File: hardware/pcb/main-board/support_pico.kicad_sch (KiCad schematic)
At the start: 8 parts, among them J701 DE15_Receptacle_HighDensity_M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, J702 Z88 SD Card, U701 Support Pico

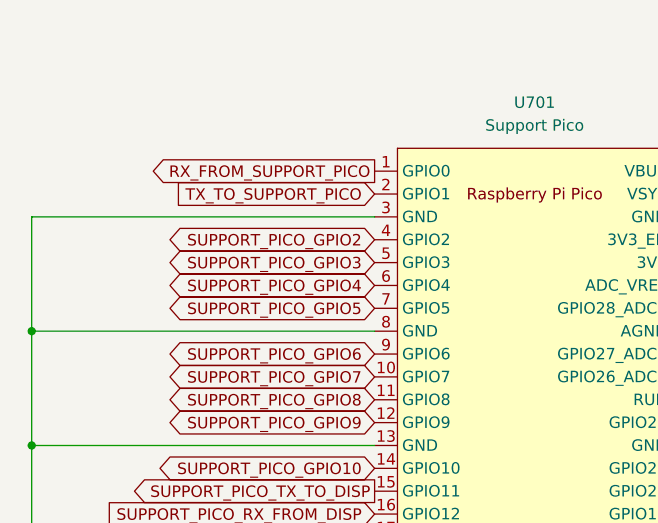
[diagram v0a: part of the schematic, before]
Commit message: start next board iteration, add latch and pico power bits
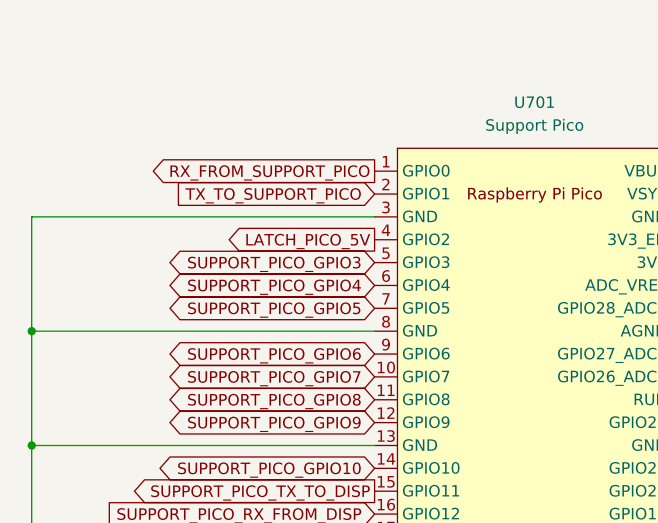
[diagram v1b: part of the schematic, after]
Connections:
- net SUPPORT_PICO_GPIO2: no longer U701.4 (GPIO2)
- new net LATCH_PICO_5V: U701.4 (GPIO2)
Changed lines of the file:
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@@
 	(title_block
 		(title "Z88R - Z88 Recreated")
-		(date "2024-08-23")
-		(rev "20240823")
+		(date "2025-12-19")
+		(rev "20251219WIP")
 		(company "Fountain and Menadue")
 	)
@@
 		)
 	)
-	(global_label "SUPPORT_PICO_GPIO2"
-		(shape bidirectional)
+	(global_label "LATCH_PICO_5V"
+		(shape output)
 		(at 58.42 43.18 180)
 		(fields_autoplaced yes)
@@
 		)
 		(property "Intersheetrefs" "${INTERSHEET_REFS}"
-			(at 34.3931 43.18 0)
+			(at 41.6956 43.18 0)
 			(effects
 				(font
@@
 		(shape output)
 		(at 58.42 76.2 180)
-		(fields_autoplaced yes)
 		(effects
 			(font
@@
 		(shape input)
 		(at 226.06 118.11 180)
-		(fields_autoplaced yes)
 		(effects
 			(font
@@
 		(shape output)
 		(at 58.42 83.82 180)
-		(fields_autoplaced yes)
 		(effects
 			(font
@@
 		(shape input)
 		(at 93.98 63.5 0)
-		(fields_autoplaced yes)
 		(effects
 			(font
@@
 		(shape input)
 		(at 93.98 68.58 0)
-		(fields_autoplaced yes)
 		(effects
 			(font
@@
 		(shape input)
 		(at 226.06 124.46 180)
-		(fields_autoplaced yes)
 		(effects
 			(font
@@
 		(shape output)
 		(at 58.42 81.28 180)
-		(fields_autoplaced yes)
-		(effects
-			(font
+		(effects
+			(font

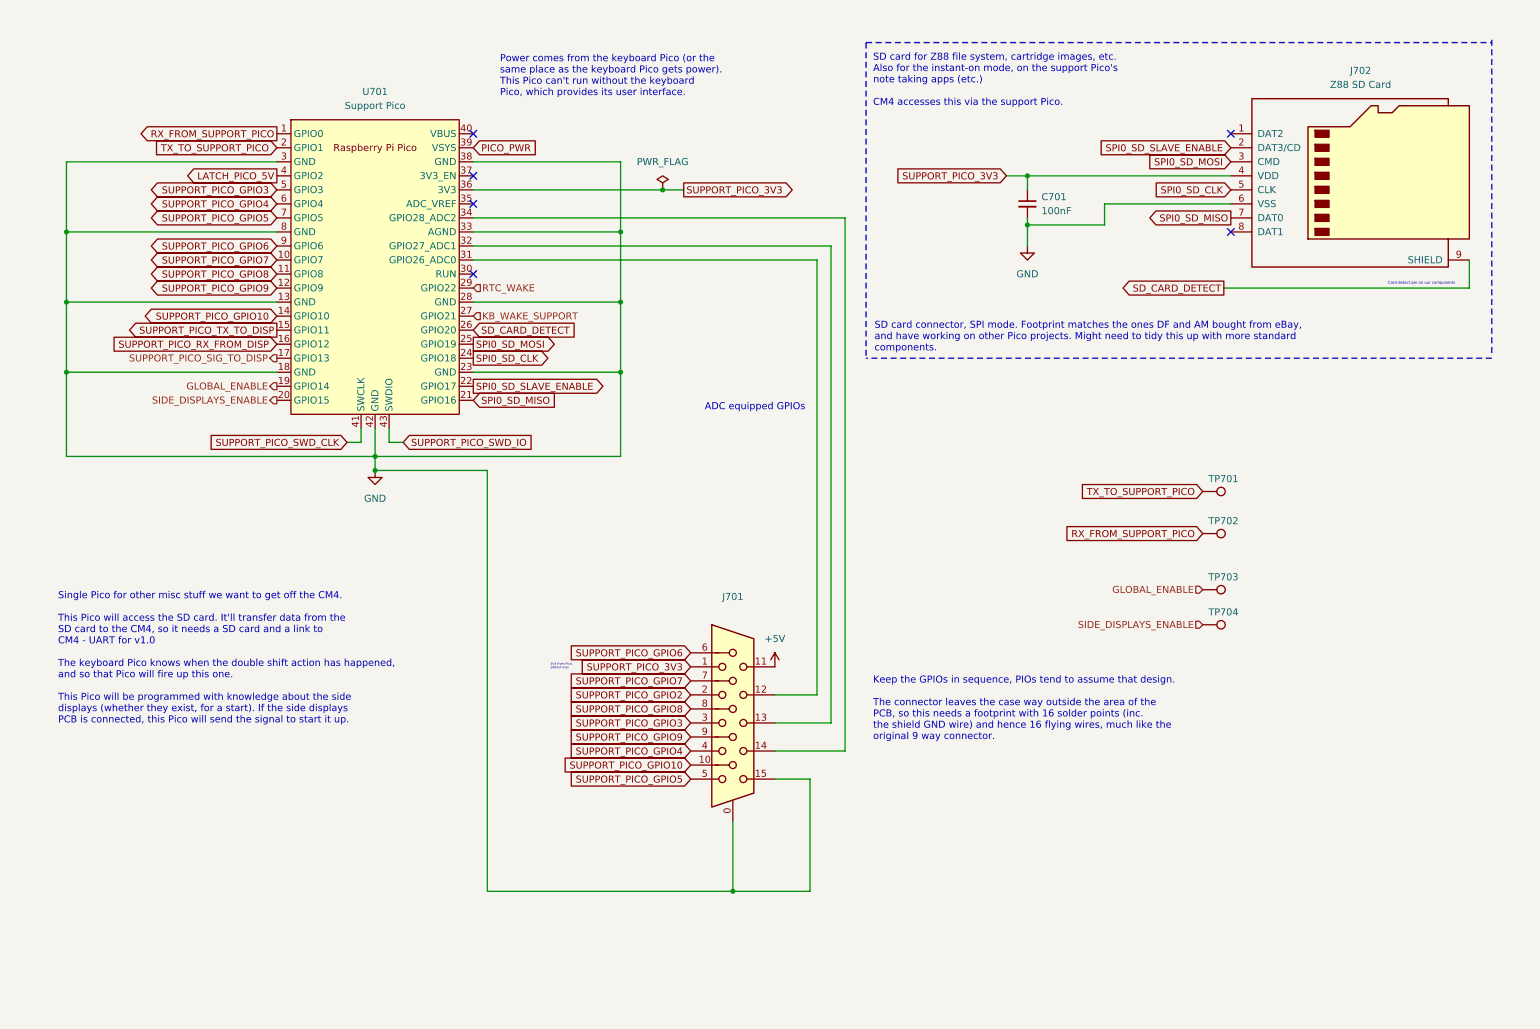
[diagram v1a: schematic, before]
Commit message: CM4 power switch
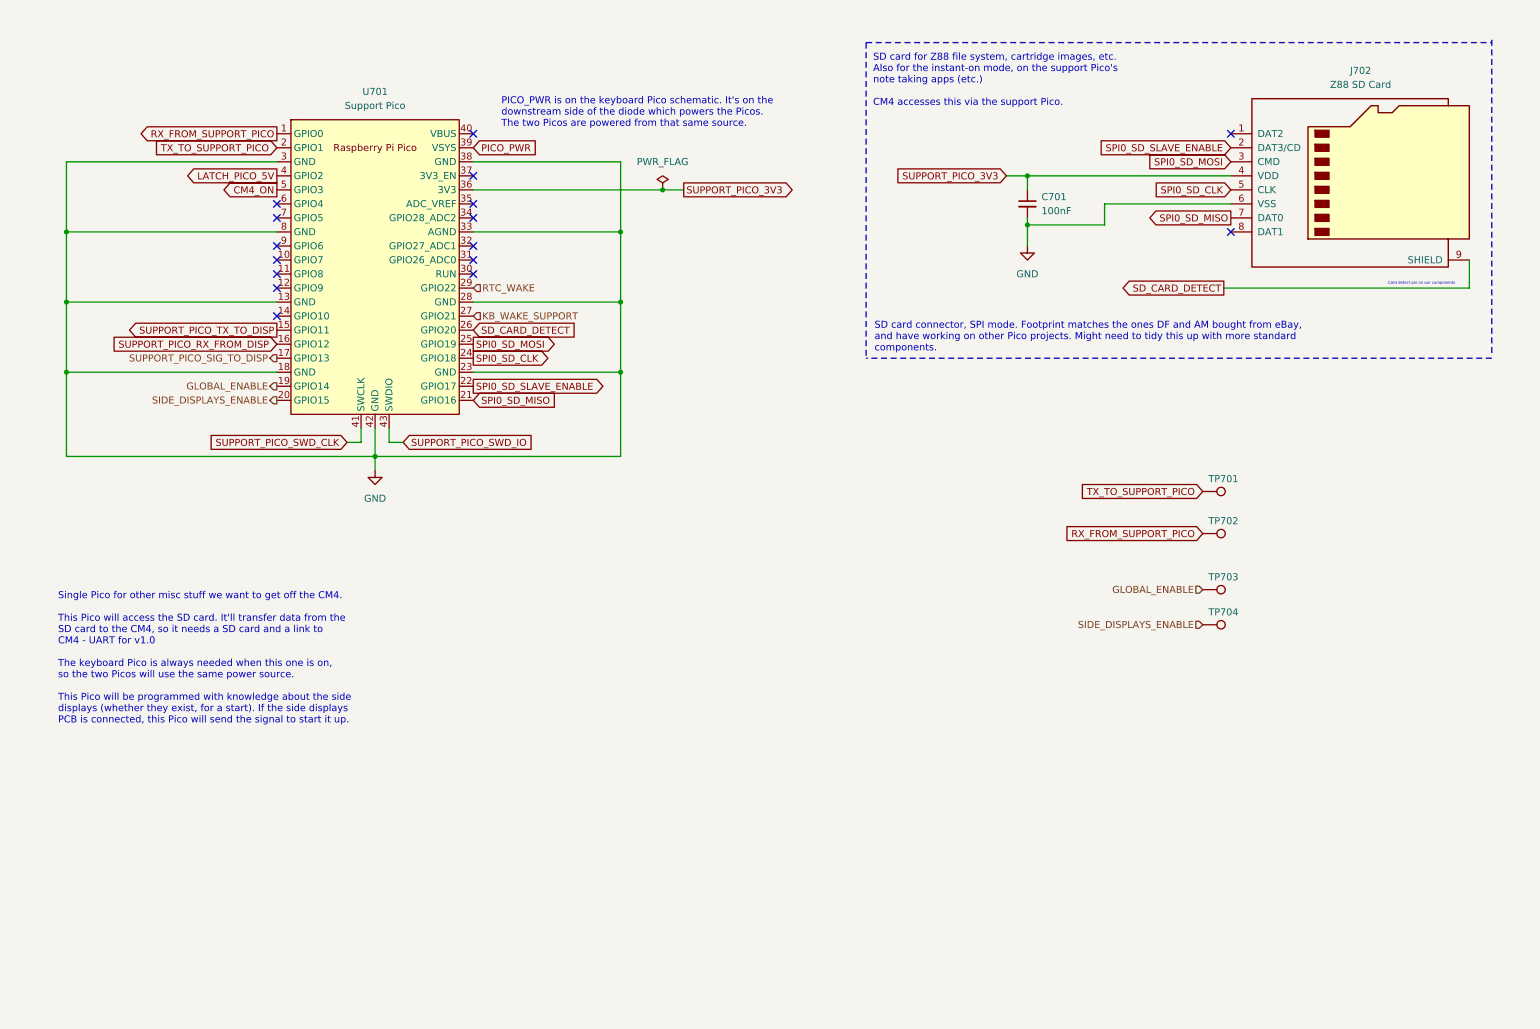
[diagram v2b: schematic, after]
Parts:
- removed J701: DE15_Receptacle_HighDensity_MountingHoles, Connector_Dsub:DSUB-15-HD_Female_Vertical_P2.29x1.98mm_MountingHoles, symbol Connector:DE15_Receptacle_HighDensity_MountingHoles
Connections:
- net SUPPORT_PICO_GPIO10: no longer names the net of U701.14 (GPIO10)
- net SUPPORT_PICO_GPIO3 renamed CM4_ON
- net SUPPORT_PICO_GPIO4: no longer names the net of U701.6 (GPIO4)
- net SUPPORT_PICO_GPIO5: no longer names the net of U701.7 (GPIO5)
- net SUPPORT_PICO_GPIO6: no longer names the net of U701.9 (GPIO6)
- net SUPPORT_PICO_GPIO7: no longer names the net of U701.10 (GPIO7)
- net SUPPORT_PICO_GPIO8: no longer names the net of U701.11 (GPIO8)
- net SUPPORT_PICO_GPIO9: no longer names the net of U701.12 (GPIO9)
- no-connect marks 6 -> 16
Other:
- note added: "PICO_PWR is on the keyboard Pico schematic. It's on the downstream side of the diode which powers the Picos. The two Picos are powered from that same source."
- note added: "Single Pico for other misc stuff we want to get off the CM4. This Pico will access the SD card. It'll transfer data from the SD card to the CM4, so it needs a SD card and a link to CM4 - UART for v1.0 The keyboard Pico is always needed when this one is on, so the two Picos will use the same power source. This Pico will be programmed with knowledge about the side displays (whether they exist, for 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"
- note removed: "3V3 from Pico, 300mA max"
- note removed: "ADC equipped GPIOs"
- note removed: "Keep the GPIOs in sequence, PIOs tend to assume that design. The connector leaves the case way outside the area of the PCB, so this needs a footprint with 16 solder points (inc. the shield GND wire) and hence 16 flying wires, much like the original 9 way connector."
- note removed: "Power comes from the keyboard Pico (or the same place as the keyboard Pico gets power). This Pico can't run without the keyboard Pico, which provides its user interface."
- note removed: "Single Pico for other misc stuff we want to get off the CM4. This Pico will access the SD card. It'll transfer data from the SD card to the CM4, so it needs a SD card and a link to CM4 - UART for v1.0 The keyboard Pico knows when the double shift action has happened, and so that Pico will fire up this one. This Pico will be programmed with knowledge about the side displays (whether they exist, fo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"

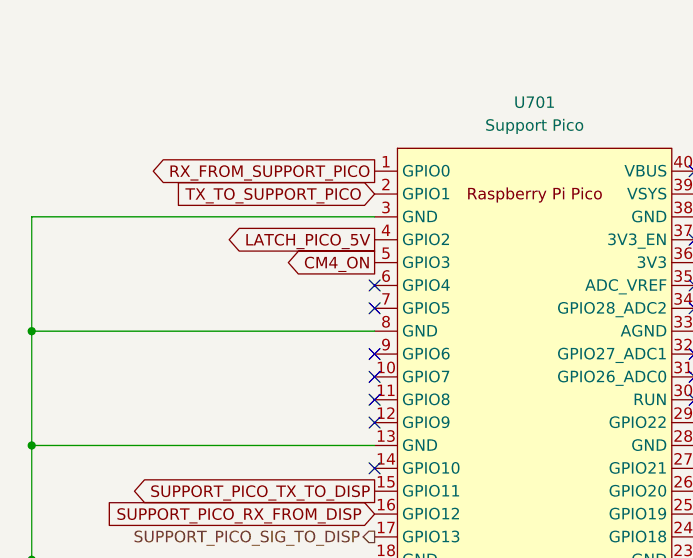
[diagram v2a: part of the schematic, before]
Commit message: add i2c connection to the support pico so it can control the RTC
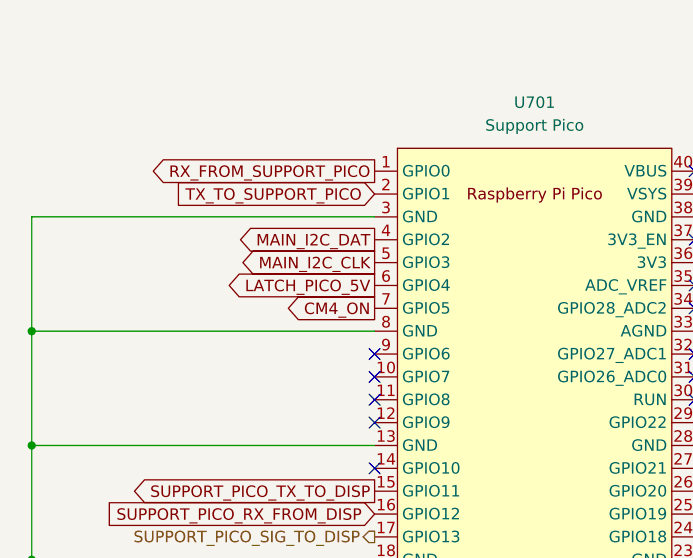
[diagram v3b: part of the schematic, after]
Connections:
- net CM4_ON: now also U701.7 (GPIO5); no longer U701.5 (GPIO3)
- net LATCH_PICO_5V: now also U701.6 (GPIO4); no longer U701.4 (GPIO2)
- new net MAIN_I2C_CLK: U701.5 (GPIO3)
- new net MAIN_I2C_DAT: U701.4 (GPIO2)
- no-connect marks 16 -> 14
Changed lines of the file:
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@@
-	)
-	(no_connect
-		(at 58.42 48.26)
 	)
 	(no_connect
@@
 	(no_connect
 		(at 58.42 55.88)
-	)
-	(no_connect
-		(at 58.42 50.8)
 	)
 	(no_connect
@@
 	(global_label "LATCH_PICO_5V"
 		(shape output)
-		(at 58.42 43.18 180)
-		(fields_autoplaced yes)
-		(effects
-			(font
-				(size 1.27 1.27)
-			)
-			(justify right)
-		)
-		(property "Intersheetrefs" "${INTERSHEET_REFS}"
-			(at 41.6956 43.18 0)
+		(at 58.42 48.26 180)
+		(fields_autoplaced yes)
+		(effects
+			(font
+				(size 1.27 1.27)
+			)
+			(justify right)
+		)
+		(property "Intersheetrefs" "${INTERSHEET_REFS}"
+			(at 41.6956 48.26 0)
 			(effects
 				(font
@@
 		)
 	)
+	(global_label "MAIN_I2C_DAT"
+		(shape output)
+		(at 58.42 43.18 180)
+		(fields_autoplaced yes)
+		(effects
+			(font
+				(size 1.27 1.27)
+			)
+			(justify right)
+		)
+		(property "Intersheetrefs" "${INTERSHEET_REFS}"
+			(at 43.268 43.18 0)
+			(effects
+				(font
+					(size 1.27 1.27)
+				)
+				(justify right)
+				(hide yes)
+			)
+		)
+	)
 	(global_label "SUPPORT_PICO_SWD_IO"
 		(shape input)
@@
 		)
 	)
+	(global_label "MAIN_I2C_CLK"
+		(shape output)
+		(at 58.42 45.72 180)
+		(fields_autoplaced yes)
+		(effects
+			(font
+				(size 1.27 1.27)
+			)
+			(justify right)
+		)
+		(property "Intersheetrefs" "${INTERSHEET_REFS}"
+			(at 43.0261 45.72 0)
+			(effects
+				(font
+					(size 1.27 1.27)
+				)
+				(justify right)
+				(hide yes)
+			)
+		)
+	)
 	(global_label "CM4_ON"
 		(shape output)
-		(at 58.42 45.72 180)
-		(fields_autoplaced yes)
-		(effects
-			(font
-				(size 1.27 1.27)
-			)
-			(justify right)
-		)
-		(property "Intersheetrefs" "${INTERSHEET_REFS}"
-			(at 48.5295 45.72 0)
-			(effects
-				(font
+		(at 58.42 50.8 180)
+		(fields_autoplaced yes)
+		(effects
+			(font
+				(size 1.27 1.27)
+			)
+			(justify right)
+		)
+		(property "Intersheetrefs" "${INTERSHEET_REFS}"
+			(at 48.5295 50.8 0)
+			(effects
+				(font

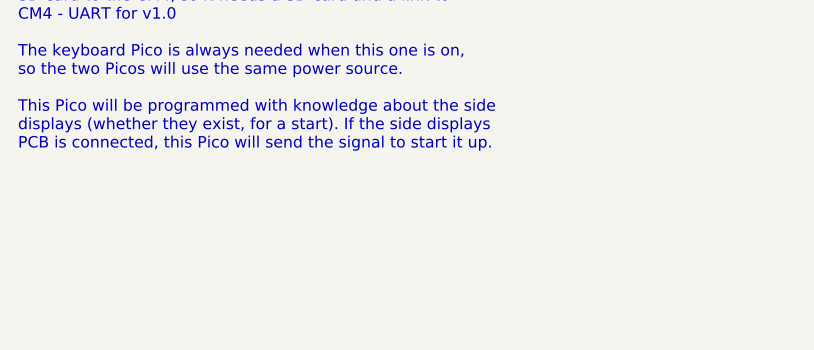
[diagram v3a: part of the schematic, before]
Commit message: turn the KB diodes round, oops
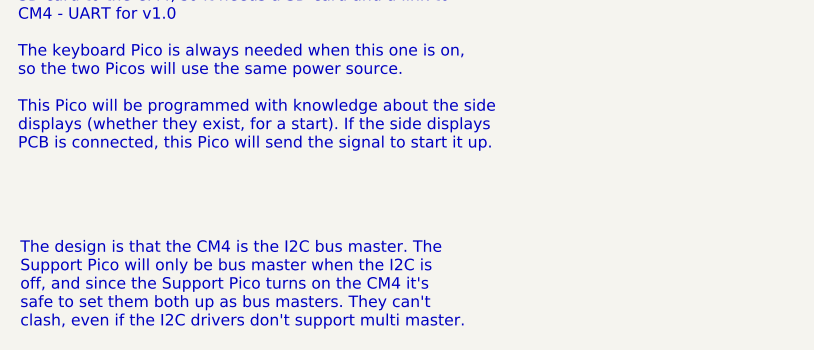
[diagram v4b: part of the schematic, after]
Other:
- note added: "The design is that the CM4 is the I2C bus master. The Support Pico will only be bus master when the I2C is off, and since the Support Pico turns on the CM4 it's safe to set them both up as bus masters. They can't clash, even if the I2C drivers don't support multi master."
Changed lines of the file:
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@@
+		)
+	)
+	(text "The design is that the CM4 is the I2C bus master. The\nSupport Pico will only be bus master when the I2C is\noff, and since the Support Pico turns on the CM4 it's\nsafe to set them both up as bus masters. They can't\nclash, even if the I2C drivers don't support multi master."
+		(exclude_from_sim no)
+		(at 19.05 157.48 0)
+		(effects
+			(font
+				(size 1.27 1.27)
+			)
+			(justify left)
 		)
 	)

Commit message: make a start on RP2040 to replace the KB pico
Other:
- title: Z88R - Z88 Recreated -> Z88R - Z88 Recreation
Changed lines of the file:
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@@
 	(paper "A4")
 	(title_block
-		(title "Z88R - Z88 Recreated")
-		(date "2025-12-19")
-		(rev "20251219WIP")
+		(title "Z88R - Z88 Recreation")
+		(date "2025-12-30")
+		(rev "20251230WIP")
 		(company "Fountain and Menadue")
 	)
